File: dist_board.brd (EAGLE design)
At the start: 80 x 80 mm, 34 parts, among them J1 2p-2.54, J10 2p-2.54, J11 2p-2.54, J12 2p-2.54, J13 2p-2.54, J14 2p-2.54, J15 2p-2.54, J16 2p-2.54, J17 2p-2.54, J18 2p-2.54, J19 4p-2.54, J2 2p-2.54, J20 4p-2.54, J21 4p-2.54, J22 4p-2.54, J3 2p-2.54, J4 2p-2.54, J5 2p-2.54, J6 2p-2.54, J7 2p-2.54, J8 2p-2.54, J9 2p-2.54, X1 BU-SMB-V, X10 BU-SMB-V, X11 BU-SMB-V, X12 BU-SMB-V, X2 BU-SMB-V, X3 BU-SMB-V, X4 BU-SMB-V, X5 BU-SMB-V, X6 BU-SMB-V, X7 BU-SMB-V, X8 BU-SMB-V, X9 BU-SMB-V

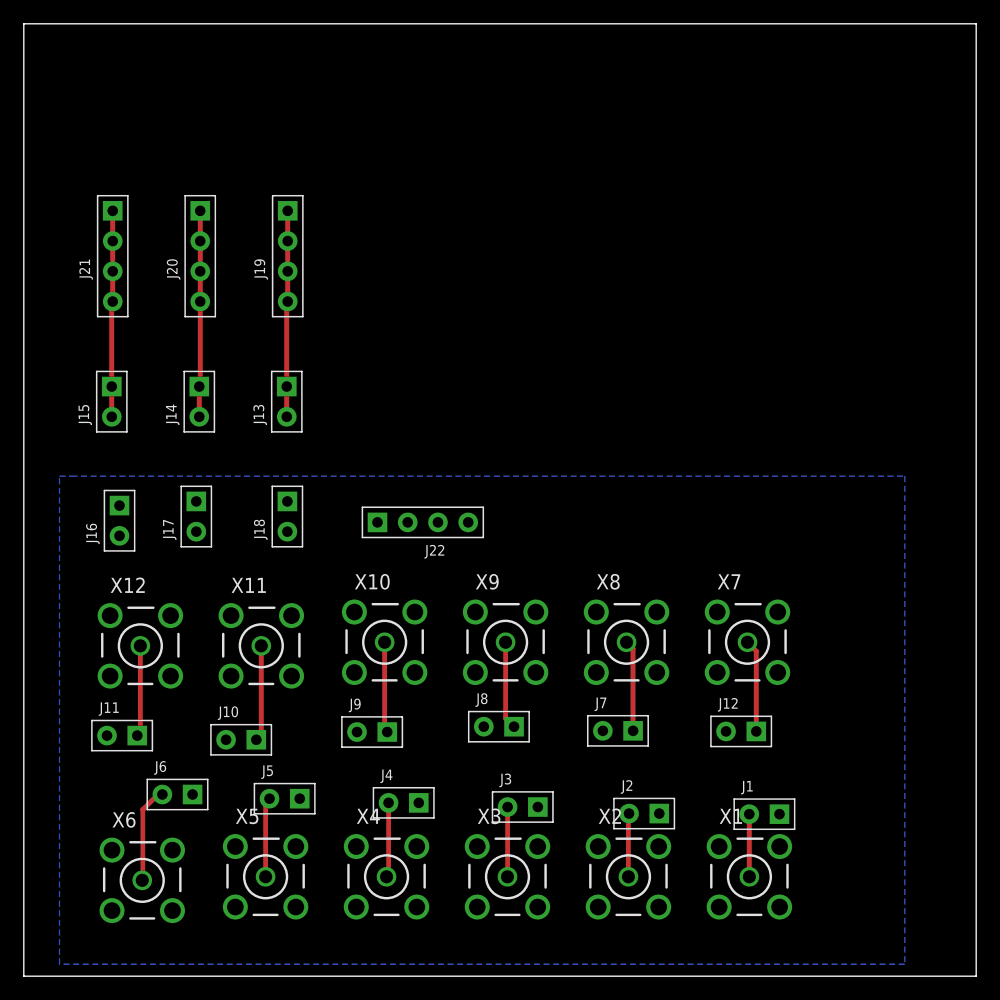
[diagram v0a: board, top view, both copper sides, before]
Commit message: cleaned up component alignment, moved HV traces up
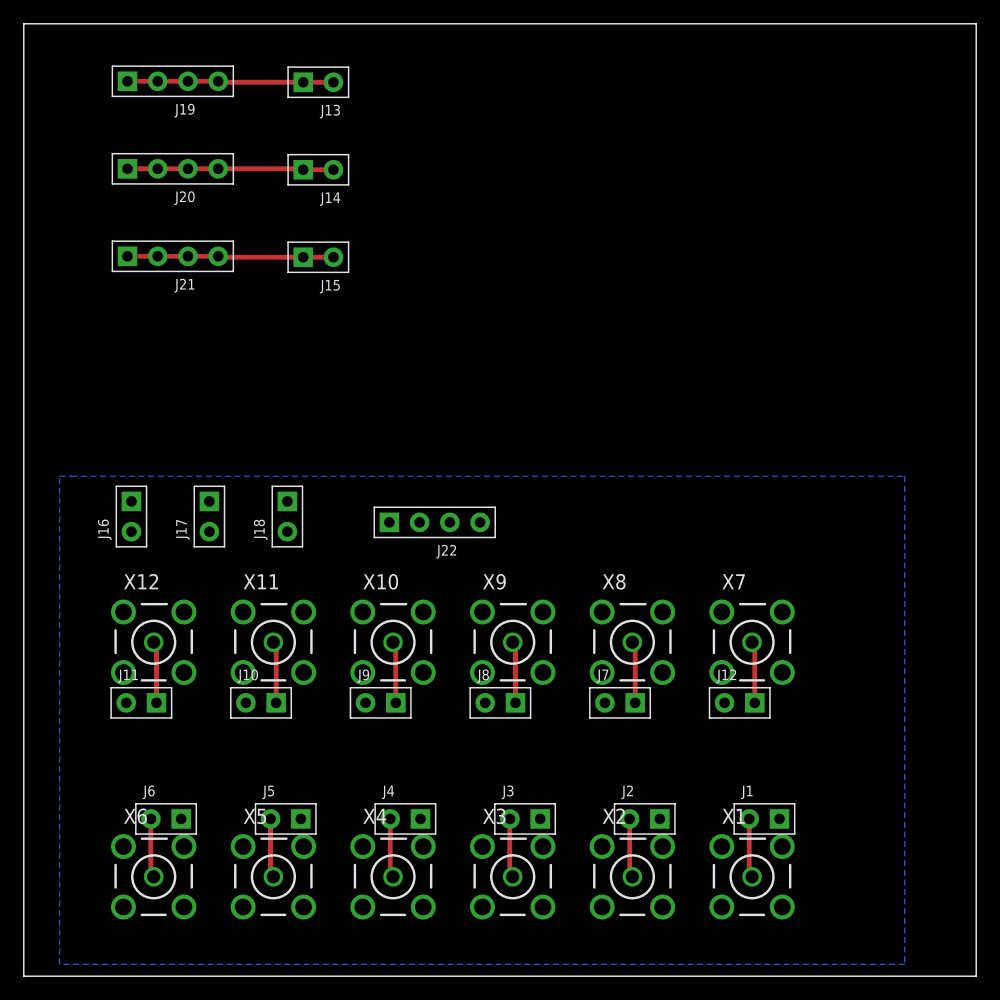
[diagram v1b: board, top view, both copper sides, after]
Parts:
- moved J13 27.0 mm to (24.7, 75.1), turned to 90 degrees
- moved J14 21.9 mm to (24.7, 67.7), turned to 90 degrees
- moved J15 21.2 mm to (24.7, 60.4), turned to 90 degrees
- moved J19 17.6 mm to (12.5, 75.2), turned to 90 degrees
- moved J20 7.69 mm to (12.5, 67.8), turned to 90 degrees
- moved J21 5.05 mm to (12.5, 60.5), turned to 90 degrees
- moved J10 3.52 mm to (19.9, 23.0)
- moved J11 3.19 mm to (9.87, 23.0)
- moved J9 2.55 mm to (30.0, 23.0)
- moved J12 2.40 mm to (60.1, 23.0)
- moved J7 2.36 mm to (50.1, 23.0)
- moved J6 2.26 mm to (11.9, 13.2)
- moved J8 2.00 mm to (40.0, 23.0)
- moved J5 1.70 mm to (22.0, 13.2)
- moved J4 1.36 mm to (32.1, 13.2)
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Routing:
- net N$3: track 8.13 -> 4.96 mm
- net N$11: track 8.06 -> 5.19 mm
- net N$13: track 7.80 -> 5.19 mm
- net N$8: track 7.67 -> 5.19 mm
- net N$12: track 7.65 -> 5.19 mm
- net N$10: track 7.63 -> 5.19 mm
- net N$9: track 7.38 -> 5.19 mm
- net N$4: track 6.70 -> 4.96 mm
- net N$5: track 6.28 -> 4.96 mm
- net N$6: track 5.86 -> 4.96 mm

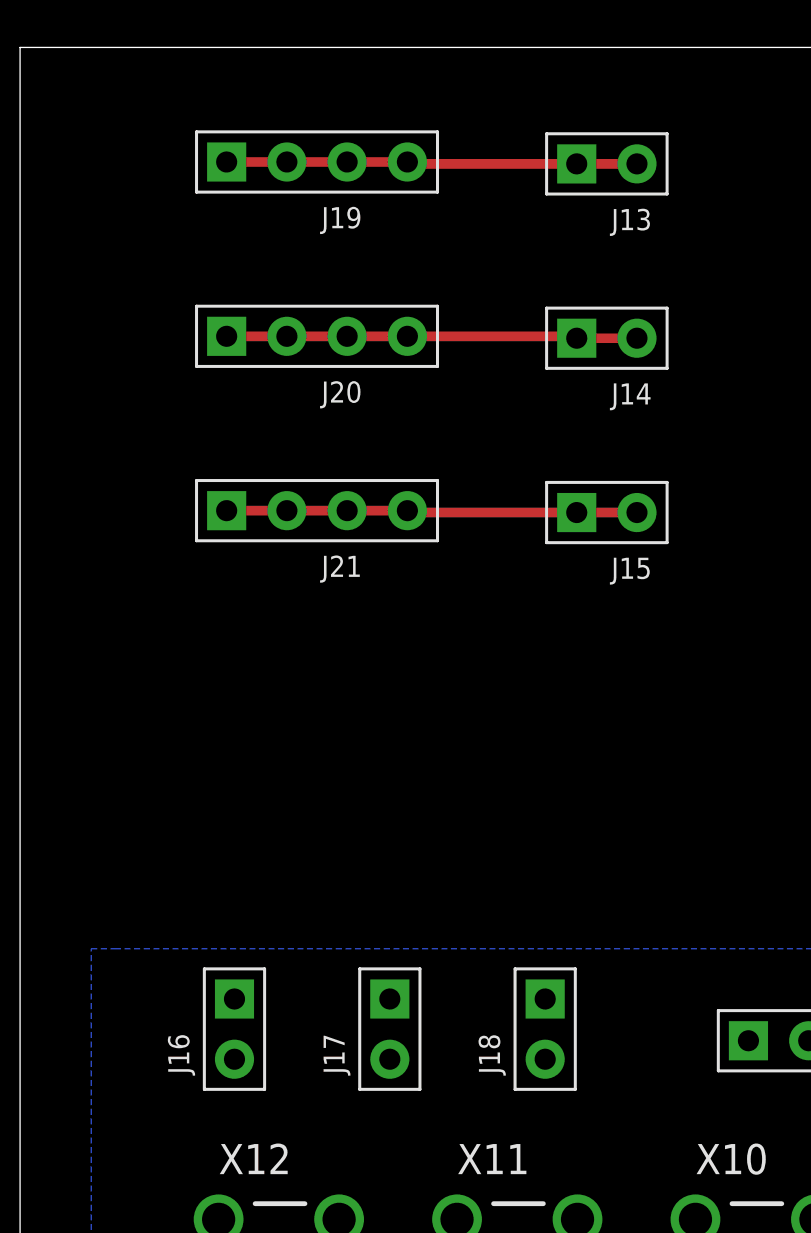
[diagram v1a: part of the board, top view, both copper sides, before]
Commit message: rotated group back, added dimension measurement
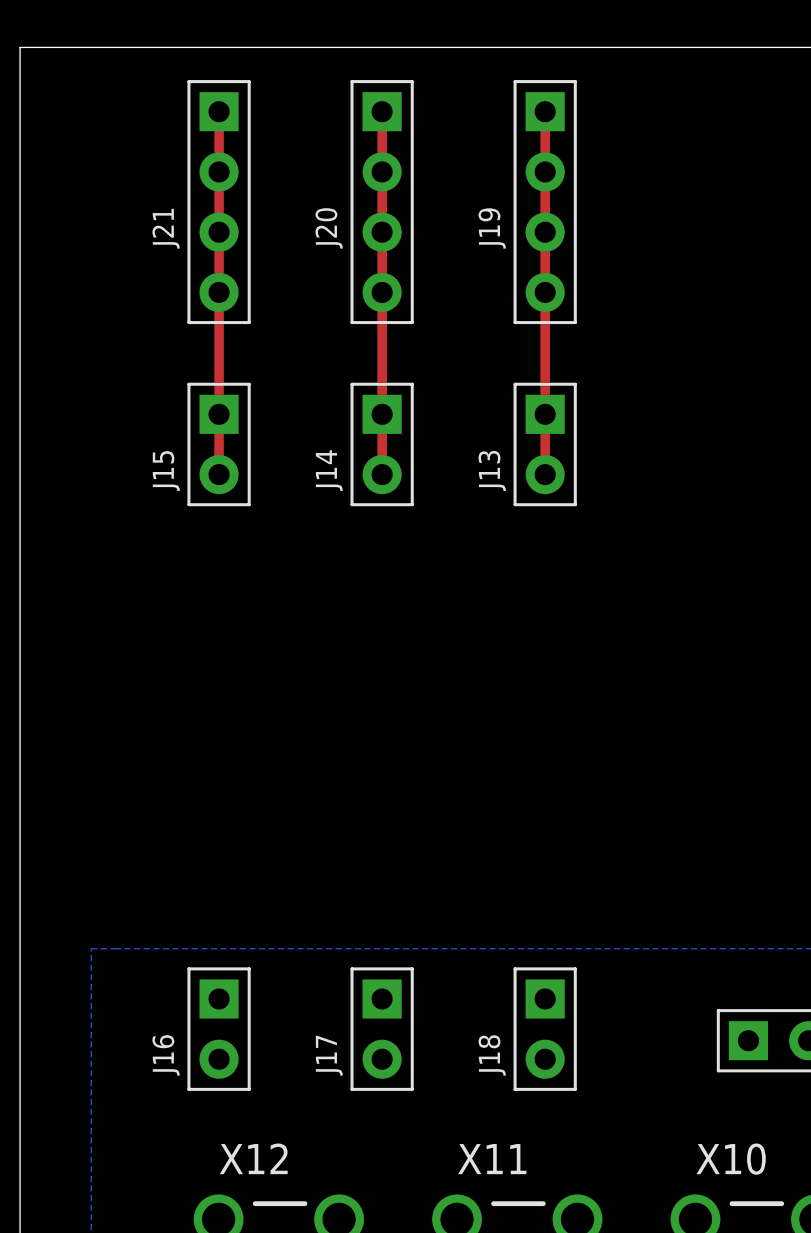
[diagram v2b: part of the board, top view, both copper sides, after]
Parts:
- moved J15 16.6 mm to (8.39, 63.3), turned to 0 degrees
- moved J21 13.6 mm to (8.39, 73.5), turned to 0 degrees
- moved J13 12.1 mm to (22.1, 63.3), turned to 0 degrees
- moved J14 10.5 mm to (15.3, 63.3), turned to 0 degrees
- moved J19 9.77 mm to (22.1, 73.5), turned to 0 degrees
- moved J20 6.29 mm to (15.3, 73.5), turned to 0 degrees
- moved J16 0.65 mm to (8.39, 38.6)
- moved J17 0.32 mm to (15.3, 38.6)
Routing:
- net N$2: track 17.9 -> 15.3 mm
- net N$18: track 17.3 -> 15.3 mm
- net N$14: track 17.3 -> 15.3 mm
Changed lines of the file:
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@@
 <dimension x1="8.4" y1="5.5" x2="13.5" y2="5.5" x3="10.95" y3="4.5" textsize="1.778" layer="1"/>
 <dimension x1="7.6" y1="5.4" x2="9.2" y2="5.4" x3="8.4" y3="6" textsize="1.778" layer="1"/>
+<dimension x1="23" y1="61" x2="23" y2="41" x3="26" y3="51" textsize="1.778" layer="1"/>
 </plain>
 <attributes>
@@
 <attribute name="MPN" value="P125-1102A0BS116A1" x="60.1354" y="22.96" size="1.778" layer="27" rot="R270" display="off"/>
 </element>
-<element name="J13" library="Seeed-Connector" library_urn="urn:adsk.eagle:library:478" package="H2-2.54" package3d_urn="urn:adsk.eagle:package:33132/1" value="2p-2.54" x="24.74" y="75.09" rot="R90">
-<attribute name="MPN" value="P125-1102A0BS116A1" x="24.74" y="75.09" size="1.778" layer="27" rot="R90" display="off"/>
-</element>
-<element name="J14" library="Seeed-Connector" library_urn="urn:adsk.eagle:library:478" package="H2-2.54" package3d_urn="urn:adsk.eagle:package:33132/1" value="2p-2.54" x="24.74" y="67.74" rot="R90">
-<attribute name="MPN" value="P125-1102A0BS116A1" x="24.74" y="67.74" size="1.778" layer="27" rot="R90" display="off"/>
-</element>
-<element name="J15" library="Seeed-Connector" library_urn="urn:adsk.eagle:library:478" package="H2-2.54" package3d_urn="urn:adsk.eagle:package:33132/1" value="2p-2.54" x="24.74" y="60.39" rot="R90">
-<attribute name="MPN" value="P125-1102A0BS116A1" x="24.74" y="60.39" size="1.778" layer="27" rot="R90" display="off"/>
-</element>
-<element name="J16" library="Seeed-Connector" library_urn="urn:adsk.eagle:library:478" package="H2-2.54" package3d_urn="urn:adsk.eagle:package:33132/1" value="2p-2.54" x="9.04" y="38.61">
-<attribute name="MPN" value="P125-1102A0BS116A1" x="9.04" y="38.61" size="1.778" layer="27" display="off"/>
-</element>
-<element name="J17" library="Seeed-Connector" library_urn="urn:adsk.eagle:library:478" package="H2-2.54" package3d_urn="urn:adsk.eagle:package:33132/1" value="2p-2.54" x="15.59" y="38.61">
-<attribute name="MPN" value="P125-1102A0BS116A1" x="15.59" y="38.61" size="1.778" layer="27" display="off"/>
+<element name="J13" library="Seeed-Connector" library_urn="urn:adsk.eagle:library:478" package="H2-2.54" package3d_urn="urn:adsk.eagle:package:33132/1" value="2p-2.54" x="22.14" y="63.26">
+<attribute name="MPN" value="P125-1102A0BS116A1" x="22.14" y="63.26" size="1.778" layer="27" display="off"/>
+</element>
+<element name="J14" library="Seeed-Connector" library_urn="urn:adsk.eagle:library:478" package="H2-2.54" package3d_urn="urn:adsk.eagle:package:33132/1" value="2p-2.54" x="15.265" y="63.26">
+<attribute name="MPN" value="P125-1102A0BS116A1" x="15.265" y="63.26" size="1.778" layer="27" display="off"/>
+</element>
+<element name="J15" library="Seeed-Connector" library_urn="urn:adsk.eagle:library:478" package="H2-2.54" package3d_urn="urn:adsk.eagle:package:33132/1" value="2p-2.54" x="8.39" y="63.26">
+<attribute name="MPN" value="P125-1102A0BS116A1" x="8.39" y="63.26" size="1.778" layer="27" display="off"/>
+</element>
+<element name="J16" library="Seeed-Connector" library_urn="urn:adsk.eagle:library:478" package="H2-2.54" package3d_urn="urn:adsk.eagle:package:33132/1" value="2p-2.54" x="8.39" y="38.61">
+<attribute name="MPN" value="P125-1102A0BS116A1" x="8.39" y="38.61" size="1.778" layer="27" display="off"/>
+</element>
+<element name="J17" library="Seeed-Connector" library_urn="urn:adsk.eagle:library:478" package="H2-2.54" package3d_urn="urn:adsk.eagle:package:33132/1" value="2p-2.54" x="15.265" y="38.61">
+<attribute name="MPN" value="P125-1102A0BS116A1" x="15.265" y="38.61" size="1.778" layer="27" display="off"/>
 </element>
 <element name="J18" library="Seeed-Connector" library_urn="urn:adsk.eagle:library:478" package="H2-2.54" package3d_urn="urn:adsk.eagle:package:33132/1" value="2p-2.54" x="22.14" y="38.61">
 <attribute name="MPN" value="P125-1102A0BS116A1" x="22.14" y="38.61" size="1.778" layer="27" display="off"/>
 </element>
-<element name="J19" library="Seeed-Connector" library_urn="urn:adsk.eagle:library:478" package="H4-2.54" package3d_urn="urn:adsk.eagle:package:33137/1" value="4p-2.54" x="12.52" y="75.17" rot="R90">
-<attribute name="MPN" value="F185-1104A1BSYA1" x="12.52" y="75.17" size="1.778" layer="27" rot="R90" display="off"/>
+<element name="J19" library="Seeed-Connector" library_urn="urn:adsk.eagle:library:478" package="H4-2.54" package3d_urn="urn:adsk.eagle:package:33137/1" value="4p-2.54" x="22.14" y="73.48">
+<attribute name="MPN" value="F185-1104A1BSYA1" x="22.14" y="73.48" size="1.778" layer="27" display="off"/>
 </element>
 <element name="J2" library="Seeed-Connector" library_urn="urn:adsk.eagle:library:478" package="H2-2.54" package3d_urn="urn:adsk.eagle:package:33132/1" value="2p-2.54" x="52.157725" y="13.21" rot="R270">
 <attribute name="MPN" value="P125-1102A0BS116A1" x="52.157725" y="13.21" size="1.778" layer="27" rot="R270" display="off"/>
 </element>
-<element name="J20" library="Seeed-Connector" library_urn="urn:adsk.eagle:library:478" package="H4-2.54" package3d_urn="urn:adsk.eagle:package:33137/1" value="4p-2.54" x="12.52" y="67.82" rot="R90">
-<attribute name="MPN" value="F185-1104A1BSYA1" x="12.52" y="67.82" size="1.778" layer="27" rot="R90" display="off"/>
-</element>
-<element name="J21" library="Seeed-Connector" library_urn="urn:adsk.eagle:library:478" package="H4-2.54" package3d_urn="urn:adsk.eagle:package:33137/1" value="4p-2.54" x="12.52" y="60.47" rot="R90">
-<attribute name="MPN" value="F185-1104A1BSYA1" x="12.52" y="60.47" size="1.778" layer="27" rot="R90" display="off"/>
+<element name="J20" library="Seeed-Connector" library_urn="urn:adsk.eagle:library:478" package="H4-2.54" package3d_urn="urn:adsk.eagle:package:33137/1" value="4p-2.54" x="15.265" y="73.48">
+<attribute name="MPN" value="F185-1104A1BSYA1" x="15.265" y="73.48" size="1.778" layer="27" display="off"/>
+</element>
+<element name="J21" library="Seeed-Connector" library_urn="urn:adsk.eagle:library:478" package="H4-2.54" package3d_urn="urn:adsk.eagle:package:33137/1" value="4p-2.54" x="8.39" y="73.48">
+<attribute name="MPN" value="F185-1104A1BSYA1" x="8.39" y="73.48" size="1.778" layer="27" display="off"/>
 </element>
 <element name="J22" library="Seeed-Connector" library_urn="urn:adsk.eagle:library:478" package="H4-2.54" package3d_urn="urn:adsk.eagle:package:33137/1" value="4p-2.54" x="34.52" y="38.12" rot="R90">
@@
 <contactref element="J19" pad="1"/>
 <contactref element="J13" pad="1"/>
-<wire x1="26.01" y1="75.09" x2="23.47" y2="75.09" width="0.4064" layer="1"/>
-<wire x1="23.47" y1="75.09" x2="16.41" y2="75.09" width="0.4064" layer="1"/>
-<wire x1="16.41" y1="75.09" x2="16.33" y2="75.17" width="0.4064" layer="1"/>
-<wire x1="16.33" y1="75.17" x2="13.79" y2="75.17" width="0.4064" layer="1"/>
-<wire x1="13.79" y1="75.17" x2="11.25" y2="75.17" width="0.4064" layer="1"/>
-<wire x1="11.25" y1="75.17" x2="8.71" y2="75.17" width="0.4064" layer="1"/>
+<wire x1="22.14" y1="69.67" x2="22.14" y2="72.21" width="0.4064" layer="1"/>
+<wire x1="22.14" y1="72.21" x2="22.14" y2="74.75" width="0.4064" layer="1"/>
+<wire x1="22.14" y1="74.75" x2="22.14" y2="77.29" width="0.4064" layer="1"/>
+<wire x1="22.14" y1="69.67" x2="22.14" y2="64.53" width="0.4064" layer="1"/>
+<wire x1="22.14" y1="64.53" x2="22.14" y2="61.99" width="0.4064" layer="1"/>
 </signal>
 <signal name="N$2">
@@
 <contactref element="J20" pad="1"/>
 <contactref element="J14" pad="1"/>
-<wire x1="26.01" y1="67.74" x2="24" y2="67.74" width="0.4064" layer="1"/>
-<wire x1="24" y1="67.74" x2="23.47" y2="67.74" width="0.4064" layer="1"/>
-<wire x1="8.71" y1="67.82" x2="11.25" y2="67.82" width="0.4064" layer="1"/>
-<wire x1="11.25" y1="67.82" x2="13.79" y2="67.82" width="0.4064" layer="1"/>
-<wire x1="13.79" y1="67.82" x2="16.33" y2="67.82" width="0.4064" layer="1"/>
-<wire x1="16.33" y1="67.82" x2="23.92" y2="67.82" width="0.4064" layer="1"/>
-<wire x1="23.92" y1="67.82" x2="24" y2="67.74" width="0.4064" layer="1"/>
+<wire x1="15.265" y1="77.29" x2="15.265" y2="74.75" width="0.4064" layer="1"/>
+<wire x1="15.265" y1="74.75" x2="15.265" y2="72.21" width="0.4064" layer="1"/>
+<wire x1="15.265" y1="72.21" x2="15.265" y2="69.67" width="0.4064" layer="1"/>
+<wire x1="15.265" y1="69.67" x2="15.265" y2="64.53" width="0.4064" layer="1"/>
+<wire x1="15.265" y1="61.99" x2="15.265" y2="64.53" width="0.4064" layer="1"/>
 </signal>
 <signal name="N$14">
@@
 <contactref element="J21" pad="2"/>
 <contactref element="J21" pad="1"/>
-<wire x1="26.01" y1="60.39" x2="23.47" y2="60.39" width="0.4064" layer="1"/>
-<wire x1="23.47" y1="60.39" x2="16.41" y2="60.39" width="0.4064" layer="1"/>
-<wire x1="16.41" y1="60.39" x2="16.33" y2="60.47" width="0.4064" layer="1"/>
-<wire x1="16.33" y1="60.47" x2="13.79" y2="60.47" width="0.4064" layer="1"/>
-<wire x1="13.79" y1="60.47" x2="11.25" y2="60.47" width="0.4064" layer="1"/>
-<wire x1="11.25" y1="60.47" x2="8.71" y2="60.47" width="0.4064" layer="1"/>
+<wire x1="8.39" y1="61.99" x2="8.39" y2="64.53" width="0.4064" layer="1"/>
+<wire x1="8.39" y1="69.67" x2="8.39" y2="72.21" width="0.4064" layer="1"/>
+<wire x1="8.39" y1="72.21" x2="8.39" y2="74.75" width="0.4064" layer="1"/>
+<wire x1="8.39" y1="74.75" x2="8.39" y2="77.29" width="0.4064" layer="1"/>
+<wire x1="8.39" y1="69.67" x2="8.39" y2="64.53" width="0.4064" layer="1"/>
 </signal>
 </signals>

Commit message: ready for ordering 1
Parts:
- removed J13, J14: 2p-2.54, Seeed-Connector:H2-2.54
- removed J22: 4p-2.54, Seeed-Connector:H4-2.54
- added GROUND: 4p-2.54, Seeed-Connector:H4-2.54
- added HV2, HV3: 2p-2.54, Seeed-Connector:H2-2.54
- moved J12 50.3 mm to (9.87, 23.0)
- moved J19 16.0 mm to (38.1, 73.5)
- moved J7 10.1 mm to (60.1, 23.0)
- moved J8 10.1 mm to (50.1, 23.0)
- moved J10 10.1 mm to (30.0, 23.0)
- moved J11 10.1 mm to (19.9, 23.0)
- moved J9 10.1 mm to (40.0, 23.0)
- moved J20 8.00 mm to (23.3, 73.5)
- renumbered J15 to HV1, J16 to GROUND1, J17 to GROUND2, J18 to GROUND3
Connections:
- net GND: now also GROUND.1, GROUND.2, GROUND.3, GROUND.4; no longer J22.1, J22.2, J22.3, J22.4
- net N$10: now also J10.1; no longer J9.1
- net N$11: now also J11.1; no longer J10.1
- net N$12: now also J12.1; no longer J11.1
- net N$13: now also J7.1; no longer J12.1
- net N$18: now also HV3.1, HV3.2; no longer J13.1, J13.2
- net N$2: now also HV2.1, HV2.2; no longer J14.1, J14.2
- net N$8: now also J8.1; no longer J7.1
- net N$9: now also J9.1; no longer J8.1
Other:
- board outline removed
